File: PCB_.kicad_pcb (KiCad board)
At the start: 2 copper layers, 58 x 34 mm, 29 parts, among them J1 ST7735, J2 DS18B20, J3 TL494, J4 INA226, J5 FAN_CTRL, J6 PWR, J7 SWD, SW1 RST, U1 STM32F030F4P6, U2 AMS1117-3.3, Y1 Crystal

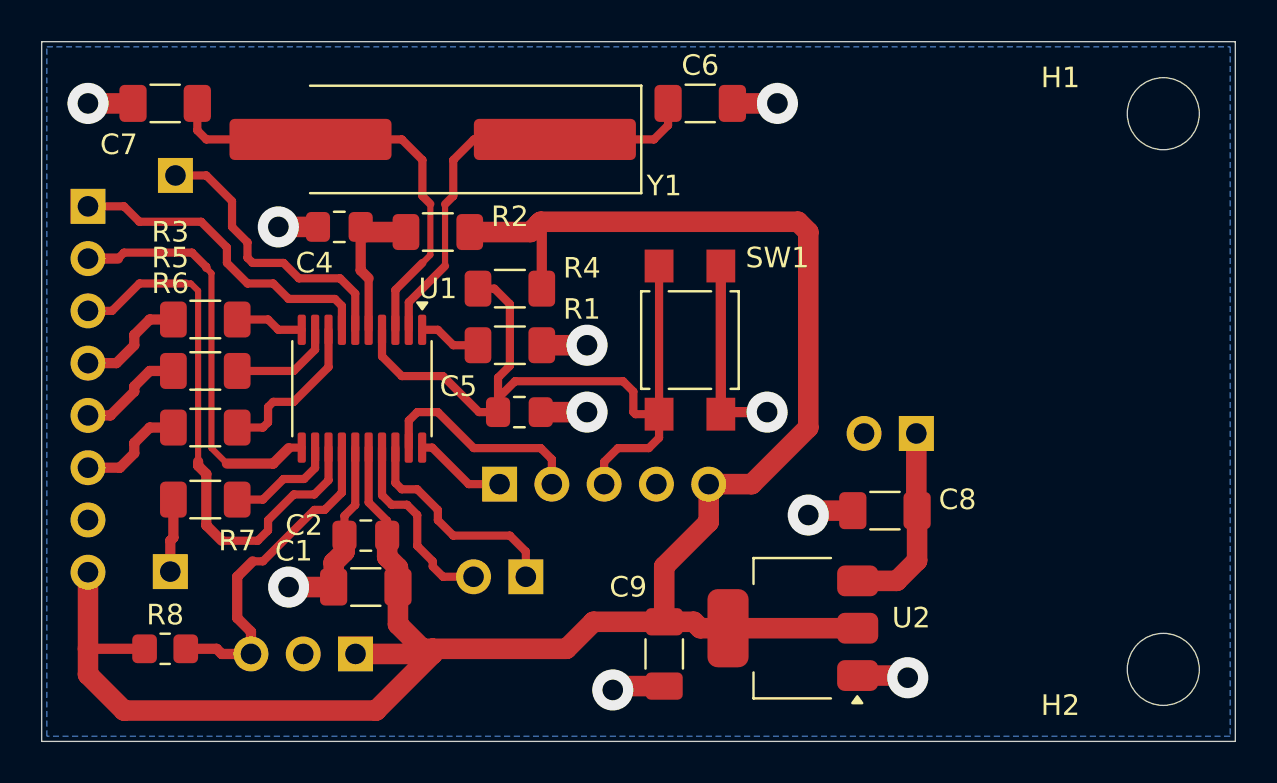
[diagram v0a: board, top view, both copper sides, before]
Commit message: DC and CS pins interconnect. The PCB is in order
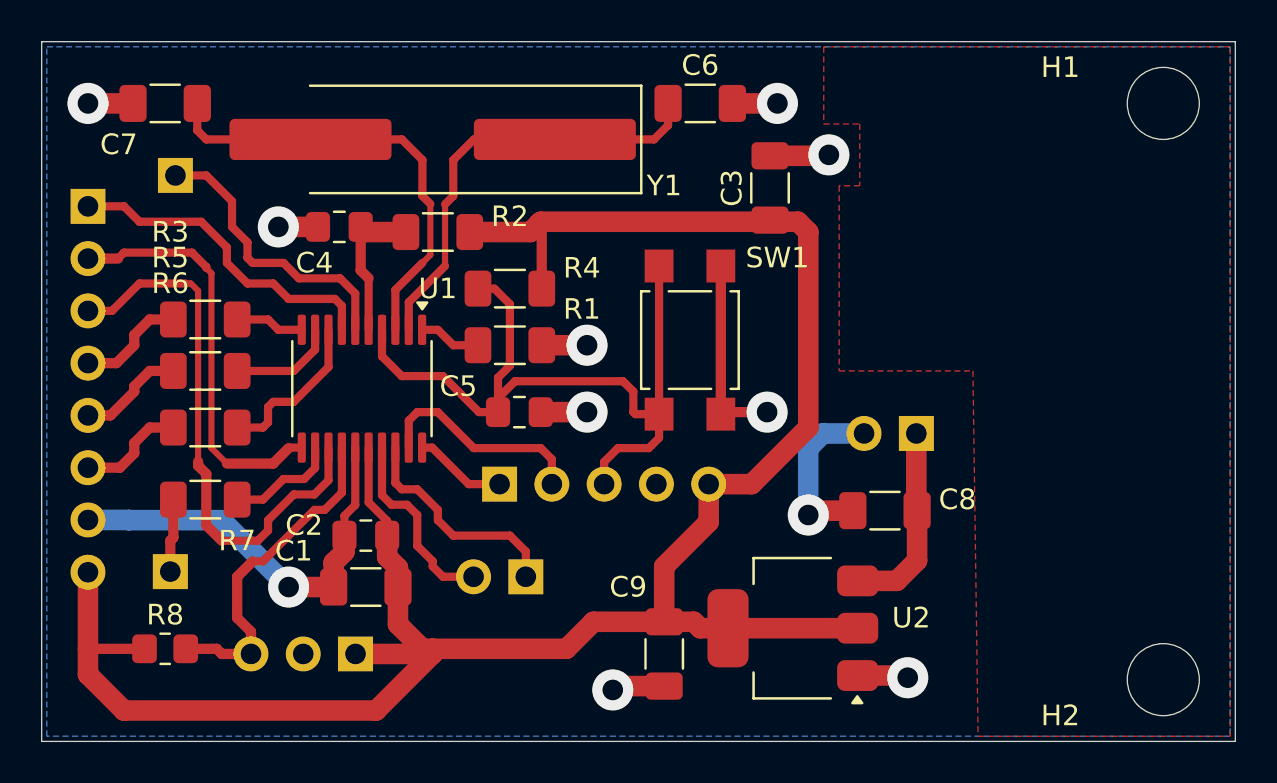
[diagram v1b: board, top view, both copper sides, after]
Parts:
- added C3: 10u, Capacitor_SMD:C_1206_3216Metric_Pad1.33x1.80mm_HandSolder, F.Cu at (181.4, 61.9)
- moved H1 0.50 mm to (200.5, 57.8)
- moved H2 0.50 mm to (200.5, 85.8)
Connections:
- R3 pad 1: DISP_CS -> DISP_DC
- R6 pad 1: DISP_DC -> DISP_CS
- U1 pad 10: DISP_CS -> DISP_DC
- U1 pad 8: DISP_DC -> DISP_CS
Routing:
- net GND: track 36.9 -> 57.2 mm, vias 10 -> 11
- net DISP_DC: track 7.91 -> 3.34 mm
- net DISP_CS: track 3.34 -> 7.91 mm
- added copper zone on F.Cu, net GND
